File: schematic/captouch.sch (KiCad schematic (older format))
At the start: 14 parts, among them P1 CONN_01X02, P2 CONN_01X04, P3 CONN_01X03, Q1 DMN3404L, U1 LD1117S33CTR, U2 MSP430G2553IPW20

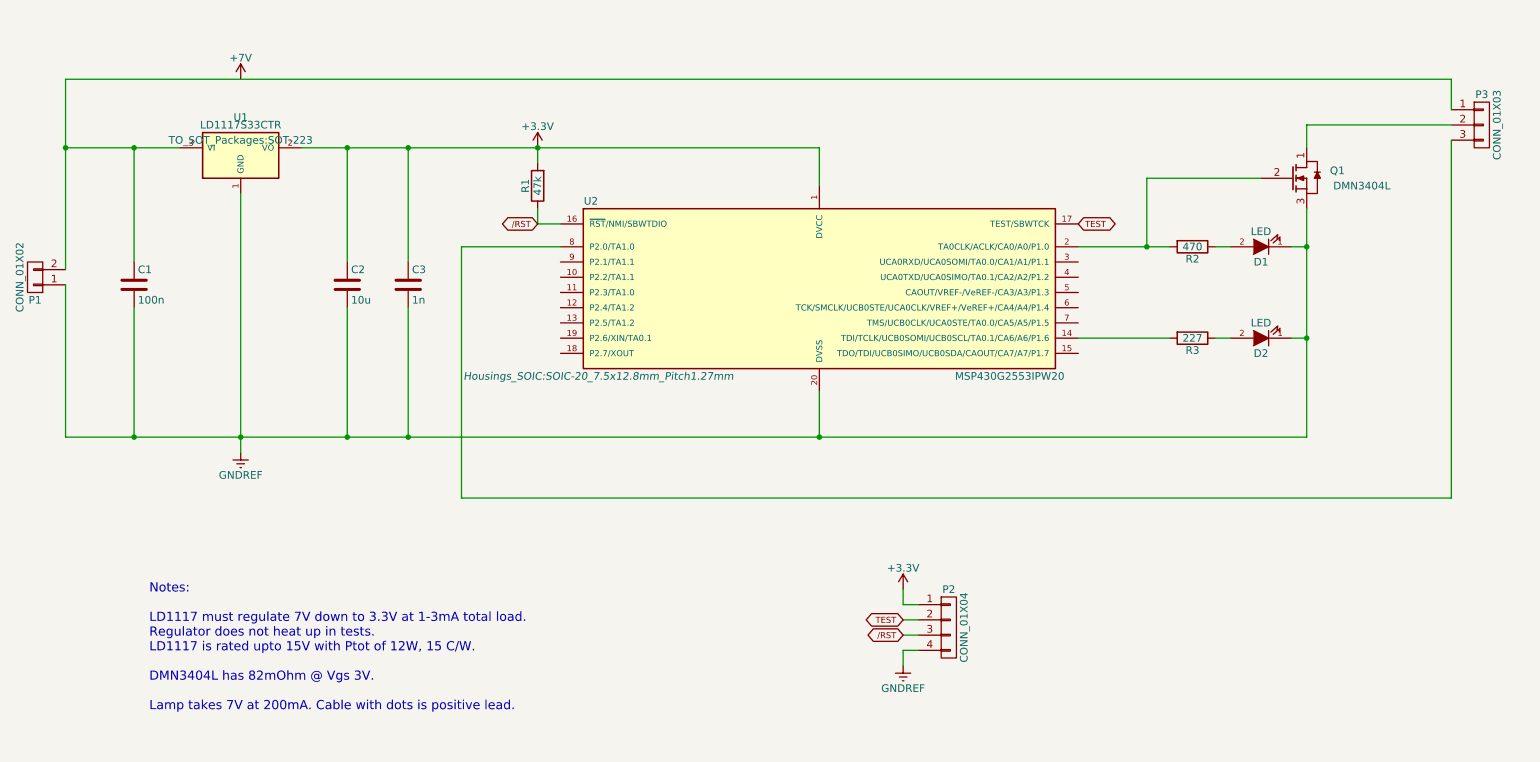
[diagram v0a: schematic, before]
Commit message: Incorporated Martins schematic comments
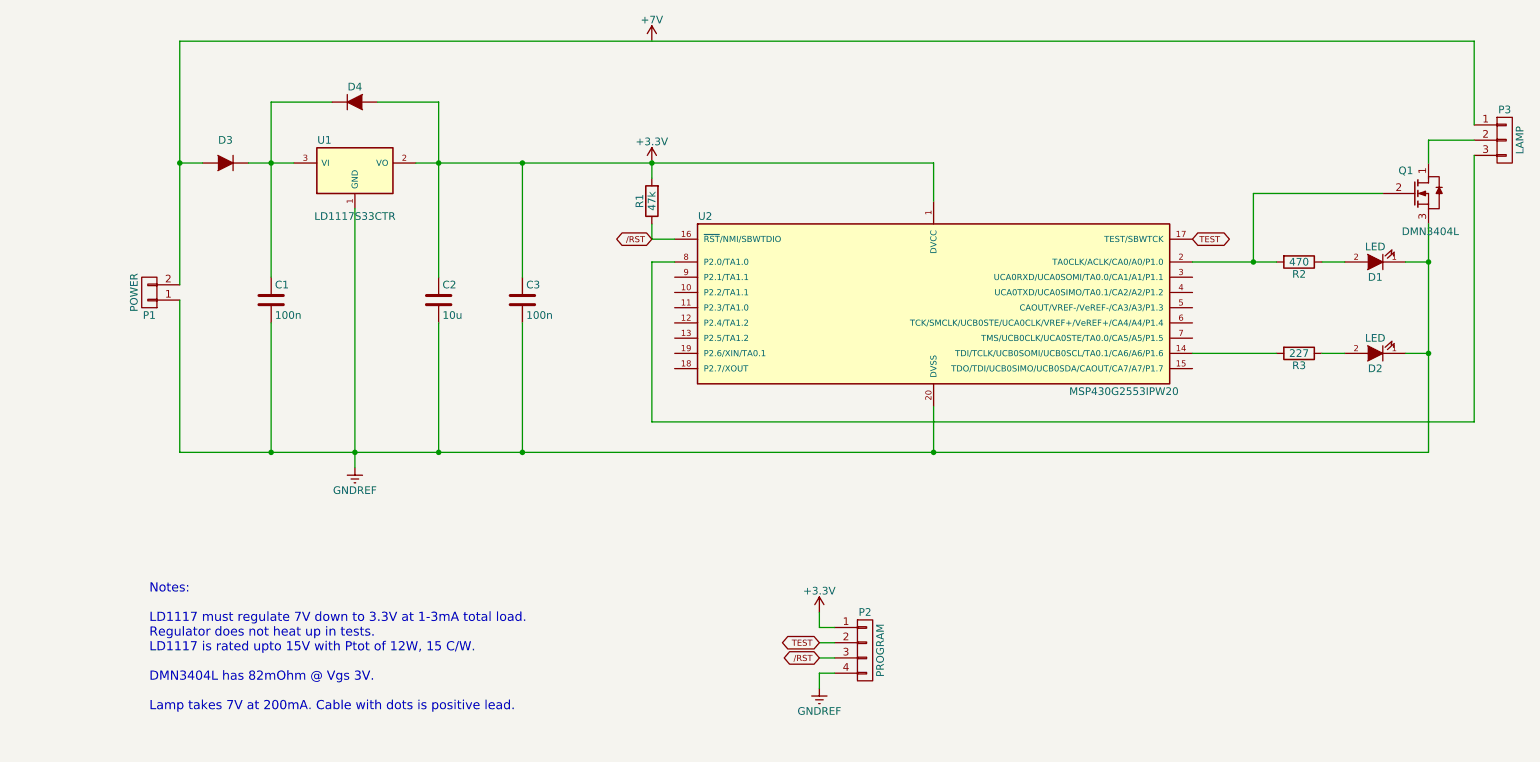
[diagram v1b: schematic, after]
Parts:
- added D3, D4: D, SMD_Packages:SMD-1206_Pol, symbol D
- C3: value 1n -> 100n
- D1, D2: footprint Diodes_SMD:SMA_Standard -> LEDs:LED_1206
- P1: value CONN_01X02 -> POWER
- P2: value CONN_01X04 -> PROGRAM
- P3: value CONN_01X03 -> LAMP
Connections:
- net +3V3: now also D4.2 (A)
- net at C1.1, U1.3 (VI): now also D3.1 (K), D4.1 (K); no longer P1.2 (P2), P3.1 (P1)
- new net: D3.2 (A), P1.2 (P2), P3.1 (P1)
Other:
- moved on the sheet: C1, C2, C3, D1, D2, P1, P2, P3, Q1, R1, R2, R3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

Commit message: More little adjustments + logo
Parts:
- removed P2: PROGRAM, Pin_Headers:Pin_Header_Angled_1x04, symbol CONN_01X04
- added P2: PROGRAM, Pin_Headers:Pin_Header_Angled_1x06, symbol CONN_01X06
- P1: footprint w_conn_mkds:mkds_1,5-2 -> conn:P_1,5-2
- P3: footprint w_conn_mkds:mkds_1,5-3 -> conn:P_1,5-3
- U2: footprint Housings_SOIC:SOIC-20_7.5x12.8mm_Pitch1.27mm -> Housings_SSOP:TSSOP-20_4.4x6.5mm_Pitch0.65mm
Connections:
- net +3V3: now also P2.1 (P1)
- net /RST: now also P2.3 (P3)
- net GNDREF: now also P2.6 (P6)
- net TEST: now also P2.2 (P2)
- net TXD: now reaches U2.3 (UCA0RXD/UCA0SOMI/TA0.0/CA1/A1/P1.1)
- net TXD: now also P2.5 (P5)
- net RXD: now reaches U2.4 (UCA0TXD/UCA0SIMO/TA0.1/CA2/A2/P1.2)
- net RXD: now also P2.4 (P4)
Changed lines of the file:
@@
 F 0 "U2" H 5100 3550 50  0000 C CNN
 F 1 "MSP430G2553IPW20" H 7850 2400 50  0000 C CNN
-F 2 "Housings_SOIC:SOIC-20_7.5x12.8mm_Pitch1.27mm" H 5150 2400 50  0001 C CIN
+F 2 "Housings_SSOP:TSSOP-20_4.4x6.5mm_Pitch0.65mm" H 5150 2400 50  0001 C CIN
 F 3 "" H 6550 2950 50  0000 C CNN
 	1    6600 2950
@@
 U 1 1 5739DD95
 P 9000 2650
-F 0 "R2" V 9080 2650 50  0000 C CNN
+F 0 "R2" V 9100 2650 50  0000 C CNN
 F 1 "470" V 9000 2650 50  0000 C CNN
 F 2 "Resistors_SMD:R_0805" V 8930 2650 50  0001 C CNN
@@
 U 1 1 5739DDE2
 P 9000 3250
-F 0 "R3" V 9080 3250 50  0000 C CNN
+F 0 "R3" V 9100 3250 50  0000 C CNN
 F 1 "227" V 9000 3250 50  0000 C CNN
 F 2 "Resistors_SMD:R_0805" V 8930 3250 50  0001 C CNN
@@
 F 0 "P1" H 1450 3000 50  0000 C CNN
 F 1 "POWER" V 1550 2850 50  0000 C CNN
-F 2 "w_conn_mkds:mkds_1,5-2" H 1450 2850 50  0001 C CNN
+F 2 "conn:P_1,5-2" H 1450 2850 50  0001 C CNN
 F 3 "" H 1450 2850 50  0000 C CNN
 	1    1450 2850
@@
 F 0 "P3" H 10350 2050 50  0000 C CNN
 F 1 "LAMP" V 10450 1850 50  0000 C CNN
-F 2 "w_conn_mkds:mkds_1,5-3" H 10350 1850 50  0001 C CNN
+F 2 "conn:P_1,5-3" H 10350 1850 50  0001 C CNN
 F 3 "" H 10350 1850 50  0000 C CNN
 	1    10350 1850
@@
 Text GLabel 4750 2500 0    40   BiDi ~ 0
 /RST
-$Comp
-L CONN_01X04 P2
-U 1 1 5739ED58
-P 6150 5200
-F 0 "P2" H 6150 5450 50  0000 C CNN
-F 1 "PROGRAM" V 6250 5200 50  0000 C CNN
-F 2 "Pin_Headers:Pin_Header_Angled_1x04" H 6150 5200 50  0001 C CNN
-F 3 "" H 6150 5200 50  0000 C CNN
-	1    6150 5200
-	1    0    0    -1
-$EndComp
 Text GLabel 5850 5150 0    40   BiDi ~ 0
 TEST
@@
 	5850 5050 5850 4950
 Wire Wire Line
-	5950 5350 5850 5350
-Wire Wire Line
-	5850 5350 5850 5450
+	5950 5550 5850 5550
+Wire Wire Line
+	5850 5550 5850 5650
 $Comp
 L +3.3V #PWR04
@@
 L GNDREF #PWR05
 U 1 1 5739EFA2
-P 5850 5450
-F 0 "#PWR05" H 5850 5200 50  0001 C CNN
-F 1 "GNDREF" H 5850 5300 50  0000 C CNN
-F 2 "" H 5850 5450 50  0000 C CNN
-F 3 "" H 5850 5450 50  0000 C CNN
-	1    5850 5450
+P 5850 5650
+F 0 "#PWR05" H 5850 5400 50  0001 C CNN
+F 1 "GNDREF" H 5850 5500 50  0000 C CNN
+F 2 "" H 5850 5650 50  0000 C CNN
+F 3 "" H 5850 5650 50  0000 C CNN
+	1    5850 5650
 	1    0    0    -1
 $EndComp
@@
 Wire Wire Line
 	9850 1850 9850 2000
+Text GLabel 8300 2750 2    40   Input ~ 0
+TXD
+Text GLabel 8300 2850 2    40   Output ~ 0
+RXD
+Text GLabel 5800 5450 0    40   Input ~ 0
+TXD
+Text GLabel 5800 5350 0    40   Output ~ 0
+RXD
+Wire Wire Line
+	5800 5450 5950 5450
+Wire Wire Line
+	5800 5350 5950 5350
+$Comp
+L CONN_01X06 P2
+U 1 1 57484A9D
+P 6150 5300
+F 0 "P2" H 6150 5650 50  0000 C CNN
+F 1 "PROGRAM" V 6250 5300 50  0000 C CNN
+F 2 "Pin_Headers:Pin_Header_Angled_1x06" H 6150 5300 50  0001 C CNN
+F 3 "" H 6150 5300 50  0000 C CNN
+	1    6150 5300
+	1    0    0    -1
+$EndComp
 $EndSCHEMATC

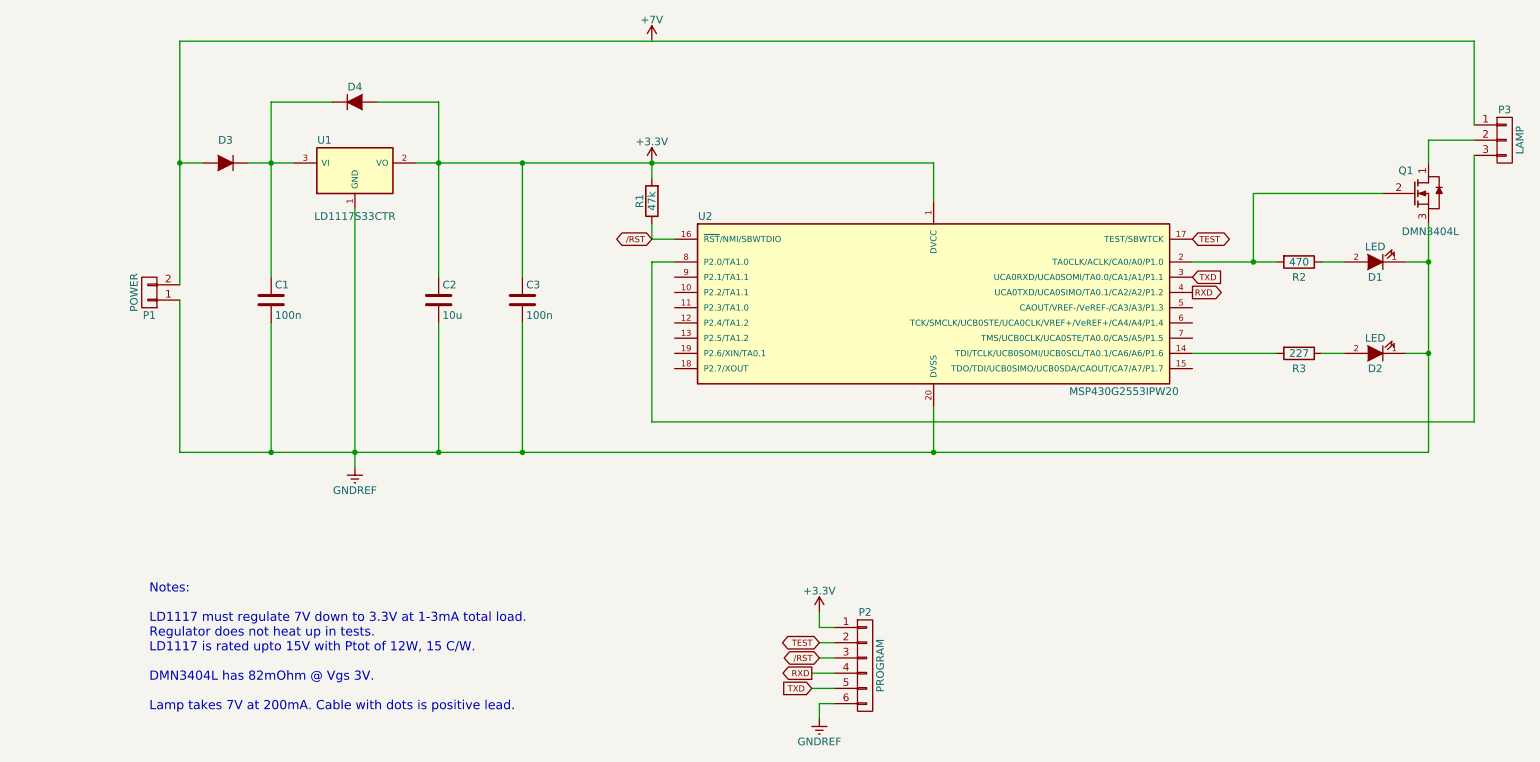
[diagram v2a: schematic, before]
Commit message: Added high pass filter
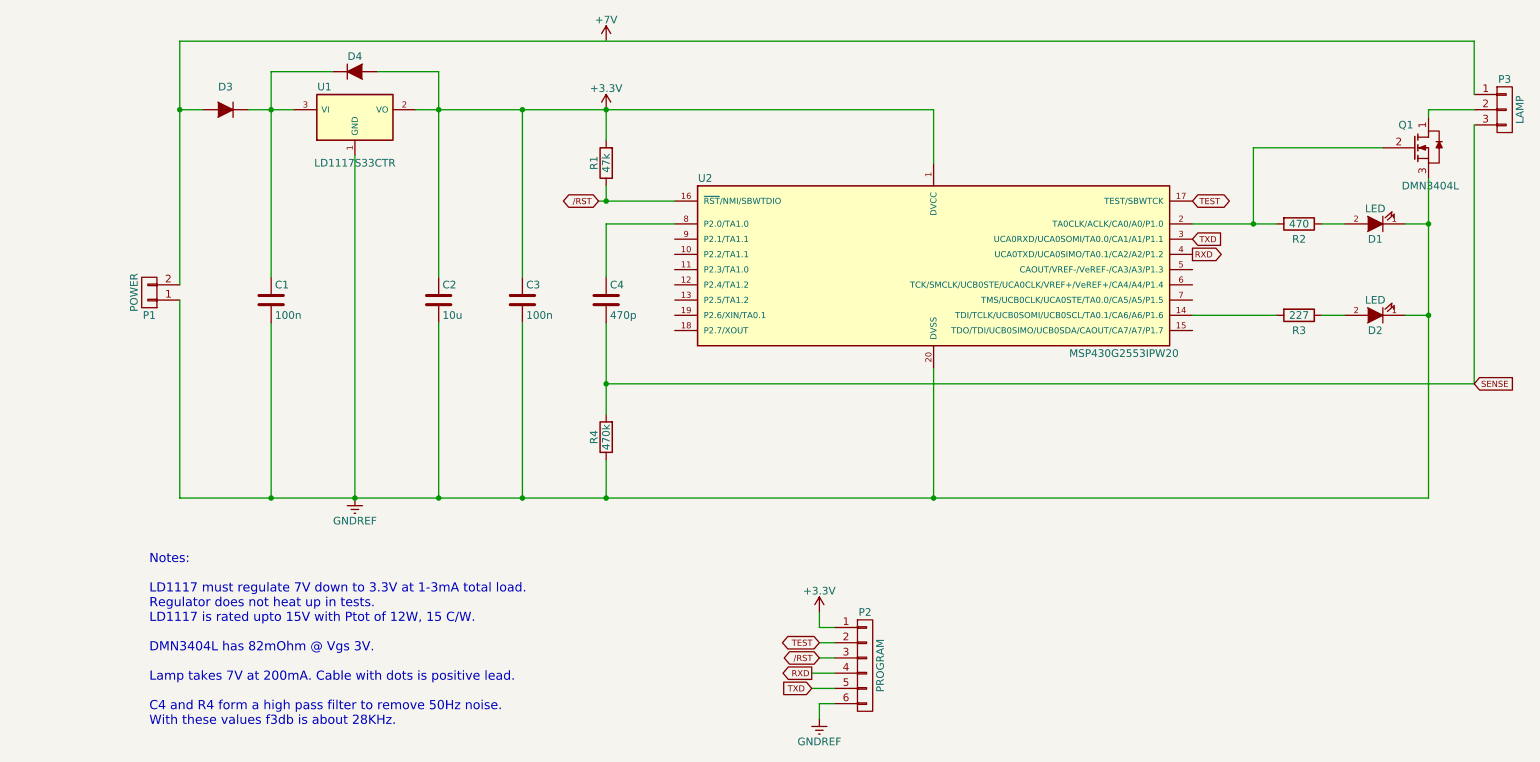
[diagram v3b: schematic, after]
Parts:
- added C4: 470p, Capacitors_SMD:C_0805, symbol C
- added R4: 470k, Resistors_SMD:R_0805, symbol R
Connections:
- net GNDREF: now also R4.1
- net at U2.8 (P2.0/TA1.0): now also C4.1; no longer P3.3 (P3)
- new net SENSE: C4.2, P3.3 (P3), R4.2
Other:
- note added: "Notes:\n\nLD1117 must regulate 7V down to 3.3V at 1-3mA total load.\nRegulator does not heat up in tests.\nLD1117 is rated upto 15V with Ptot of 12W, 15 C/W.\n\nDMN3404L has 82mOhm @ Vgs 3V.\n\nLamp takes 7V at 200mA. Cable with dots is positive lead.\n\nC4 and R4 form a high pass filter to remove 50Hz noise. \nWith these values f3db is about 28KHz."
- note removed: "Notes:\n\nLD1117 must regulate 7V down to 3.3V at 1-3mA total load.\nRegulator does not heat up in tests.\nLD1117 is rated upto 15V with Ptot of 12W, 15 C/W.\n\nDMN3404L has 82mOhm @ Vgs 3V.\n\nLamp takes 7V at 200mA. Cable with dots is positive lead.\n\n"
- moved on the sheet: D1, D2, D3, D4, P3, Q1, R1, R2, R3, U1, U2

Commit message: Update schematic to kicad 6
I wanted renders of the schematics, so adjusted all components to
kicad standard components. This way we also get to the associated 3d
models.
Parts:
- C1, C2, C3, C4: symbol C -> device:C
- D1, D2: symbol LED -> device:LED
- D3, D4: symbol D -> device:D
- P1: symbol CONN_01X02 -> conn:CONN_01X02
- P2: symbol CONN_01X06 -> conn:CONN_01X06
- P3: symbol CONN_01X03 -> conn:CONN_01X03
- Q1: symbol DMN3404L -> capacitive_touch:DMN3404L
- R1, R2, R3, R4: symbol R -> device:R
- U1: symbol LD1117S33CTR -> regul:LD1117S33CTR
- U2: symbol MSP430G2553IPW20 -> msp430:MSP430G2553IPW20
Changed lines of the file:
@@
-EESchema Schematic File Version 2
-LIBS:power
-LIBS:device
-LIBS:conn
-LIBS:linear
-LIBS:regul
-LIBS:74xx
-LIBS:cmos4000
-LIBS:adc-dac
-LIBS:memory
-LIBS:xilinx
-LIBS:microcontrollers
-LIBS:dsp
-LIBS:microchip
-LIBS:analog_switches
-LIBS:motorola
-LIBS:texas
-LIBS:intel
-LIBS:audio
-LIBS:interface
-LIBS:digital-audio
-LIBS:philips
-LIBS:display
-LIBS:cypress
-LIBS:siliconi
-LIBS:opto
-LIBS:atmel
-LIBS:contrib
-LIBS:valves
-LIBS:msp430
-LIBS:capacitive_touch
+EESchema Schematic File Version 4
 LIBS:captouch-cache
-EELAYER 25 0
+EELAYER 26 0
 EELAYER END
 $Descr A4 11693 8268
@@
 $EndDescr
 $Comp
-L MSP430G2553IPW20 U2
+L msp430:MSP430G2553IPW20 U2
 U 1 1 5739D7AE
 P 6600 2700
@@
 $EndComp
 $Comp
-L LED D1
+L device:LED D1
 U 1 1 5739DBD0
 P 9500 2400
@@
 $EndComp
 $Comp
-L LED D2
+L device:LED D2
 U 1 1 5739DD57
 P 9500 3000
@@
 $EndComp
 $Comp
-L R R2
+L device:R R2
 U 1 1 5739DD95
 P 9000 2400
@@
 $EndComp
 $Comp
-L R R3
+L device:R R3
 U 1 1 5739DDE2
 P 9000 3000
@@
 $EndComp
 $Comp
-L LD1117S33CTR U1
+L regul:LD1117S33CTR U1
 U 1 1 5739DE31
 P 2800 1700
@@
 $EndComp
 $Comp
-L C C1
+L device:C C1
 U 1 1 5739DECC
 P 2250 2900
@@
 $EndComp
 $Comp
-L C C2
+L device:C C2
 U 1 1 5739DF2C
 P 3350 2900
@@
 $EndComp
 $Comp
-L DMN3404L Q1
+L capacitive_touch:DMN3404L Q1
 U 1 1 5739E4BE
 P 9750 1900
@@
 $EndComp
 Wire Wire Line
-	8300 2400 8850 2400
+	8300 2400 8700 2400
 Wire Wire Line
 	9150 2400 9300 2400
@@
 	8850 3000 8300 3000
 Wire Wire Line
-	9850 4200 1650 4200
+	9850 4200 6600 4200
 Wire Wire Line
 	6600 3350 6600 4200
@@
 Connection ~ 6600 4200
 Wire Wire Line
-	3200 1650 6600 1650
-Wire Wire Line
-	6600 2000 6600 2000
-Wire Wire Line
-	3350 1400 3350 2750
+	3200 1650 3350 1650
+Wire Wire Line
+	3350 1400 3350 1650
 Connection ~ 3350 1650
 Wire Wire Line
@@
 Connection ~ 3350 4200
 Wire Wire Line
-	2250 1400 2250 2750
+	2250 1400 2250 1650
 Wire Wire Line
 	2250 3050 2250 4200
 Connection ~ 2800 4200
 $Comp
-L CONN_01X02 P1
+L conn:CONN_01X02 P1
 U 1 1 5739E734
 P 1450 2850
@@
 $EndComp
 $Comp
-L CONN_01X03 P3
+L conn:CONN_01X03 P3
 U 1 1 5739E80B
 P 10350 1650
@@
 	4450 2400 4900 2400
 $Comp
-L +3.3V #PWR01
+L power:+3.3V #PWR01
 U 1 1 5739E5AC
 P 4450 1650
@@
 $EndComp
 $Comp
-L +7V #PWR02
+L capacitive_touch:+7V #PWR02
 U 1 1 5739E70B
 P 4450 1200
@@
 $EndComp
 $Comp
-L GNDREF #PWR03
+L power:GNDREF #PWR03
 U 1 1 5739E78C
 P 2800 4200
@@
 $EndComp
 Wire Wire Line
-	9850 2100 9850 4200
+	9850 2100 9850 2400
 Wire Wire Line
 	9850 3000 9700 3000
@@
 Notes:\n\nLD1117 must regulate 7V down to 3.3V at 1-3mA total load.\nRegulator does not heat up in tests.\nLD1117 is rated upto 15V with Ptot of 12W, 15 C/W.\n\nDMN3404L has 82mOhm @ Vgs 3V.\n\nLamp takes 7V at 200mA. Cable with dots is positive lead.\n\nC4 and R4 form a high pass filter to remove 50Hz noise. \nWith these values f3db is about 28KHz.
 $Comp
-L R R1
+L device:R R1
 U 1 1 5739EBAB
 P 4450 2000
@@
 $EndComp
 Wire Wire Line
-	4400 2250 4900 2250
+	4400 2250 4450 2250
 Text GLabel 8300 2250 2    40   BiDi ~ 0
 TEST
@@
 	5850 5550 5850 5650
 $Comp
-L +3.3V #PWR04
+L power:+3.3V #PWR04
 U 1 1 5739EF42
 P 5850 4950
@@
 $EndComp
 $Comp
-L GNDREF #PWR05
+L power:GNDREF #PWR05
 U 1 1 5739EFA2
 P 5850 5650
@@
 $EndComp
 $Comp
-L C C3
+L device:C C3
 U 1 1 5739F103
 P 3900 2900
@@
 Connection ~ 3900 4200
 $Comp
-L D D4
+L device:D D4
 U 1 1 57432C26
 P 2800 1400
@@
 $EndComp
 $Comp
-L D D3
+L device:D D3
 U 1 1 57432D3D
 P 1950 1650
@@
 $EndComp
 Wire Wire Line
-	1650 1200 1650 2800
+	1650 1200 1650 1650
 Connection ~ 1650 1650
 Wire Wire Line
@@
 	2650 1400 2250 1400
 Wire Wire Line
-	2100 1650 2400 1650
+	2100 1650 2250 1650
 Wire Wire Line
 	1800 1650 1650 1650
@@
 	5800 5350 5950 5350
 $Comp
-L CONN_01X06 P2
+L conn:CONN_01X06 P2
 U 1 1 57484A9D
 P 6150 5300
@@
 $EndComp
 $Comp
-L C C4
+L device:C C4
 U 1 1 57D59CD2
 P 4450 2900
@@
 $EndComp
 $Comp
-L R R4
+L device:R R4
 U 1 1 57D59E06
 P 4450 3800
@@
 $EndComp
 Wire Wire Line
-	4450 3050 4450 3650
+	4450 3050 4450 3450
 Wire Wire Line
 	4450 3950 4450 4200
@@
 Text GLabel 10150 3450 2    40   Input ~ 0
 SENSE
+Wire Wire Line
+	8700 2400 8850 2400
+Wire Wire Line
+	6600 4200 4450 4200
+Wire Wire Line
+	3350 1650 3900 1650
+Wire Wire Line
+	3350 1650 3350 2750
+Wire Wire Line
+	3350 4200 2800 4200
+Wire Wire Line
+	2800 4200 2250 4200
+Wire Wire Line
+	2250 1650 2250 2750
+Wire Wire Line
+	2250 1650 2400 1650
+Wire Wire Line
+	2250 4200 1650 4200
+Wire Wire Line
+	9850 3000 9850 4200
+Wire Wire Line
+	9850 2400 9850 3000
+Wire Wire Line
+	3900 1650 4450 1650
+Wire Wire Line
+	3900 4200 3350 4200
+Wire Wire Line
+	1650 1650 1650 2800
+Wire Wire Line
+	4450 4200 3900 4200
+Wire Wire Line
+	4450 1650 6600 1650
+Wire Wire Line
+	4450 2250 4900 2250
+Wire Wire Line
+	4450 3450 4450 3650
 $EndSCHEMATC
